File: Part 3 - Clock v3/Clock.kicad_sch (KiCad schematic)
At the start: 77 parts, among them SW2 MODE, SW3 SPEED, SW4 STEP, SW5 BOOT SPEED, SW6 BOOT MODE, SW7 SW_DIP_x08, SW8 RESET FAST LSB, SW9 RESET FAST MSB, U1 74AHC14, U10 74HC112, U11 74AHC74, U12 LMC555, U13 74HC251, U14 74HC40103, U15 74AHC138, U16 74HC251, U17 74HC251, U3 74AHC08, U4 74AHC14, U5 74AHC74, U6 74AHC74, U7 74AHC74, U8 74AHC74, U9 74HC112, X1 14.7456MHz

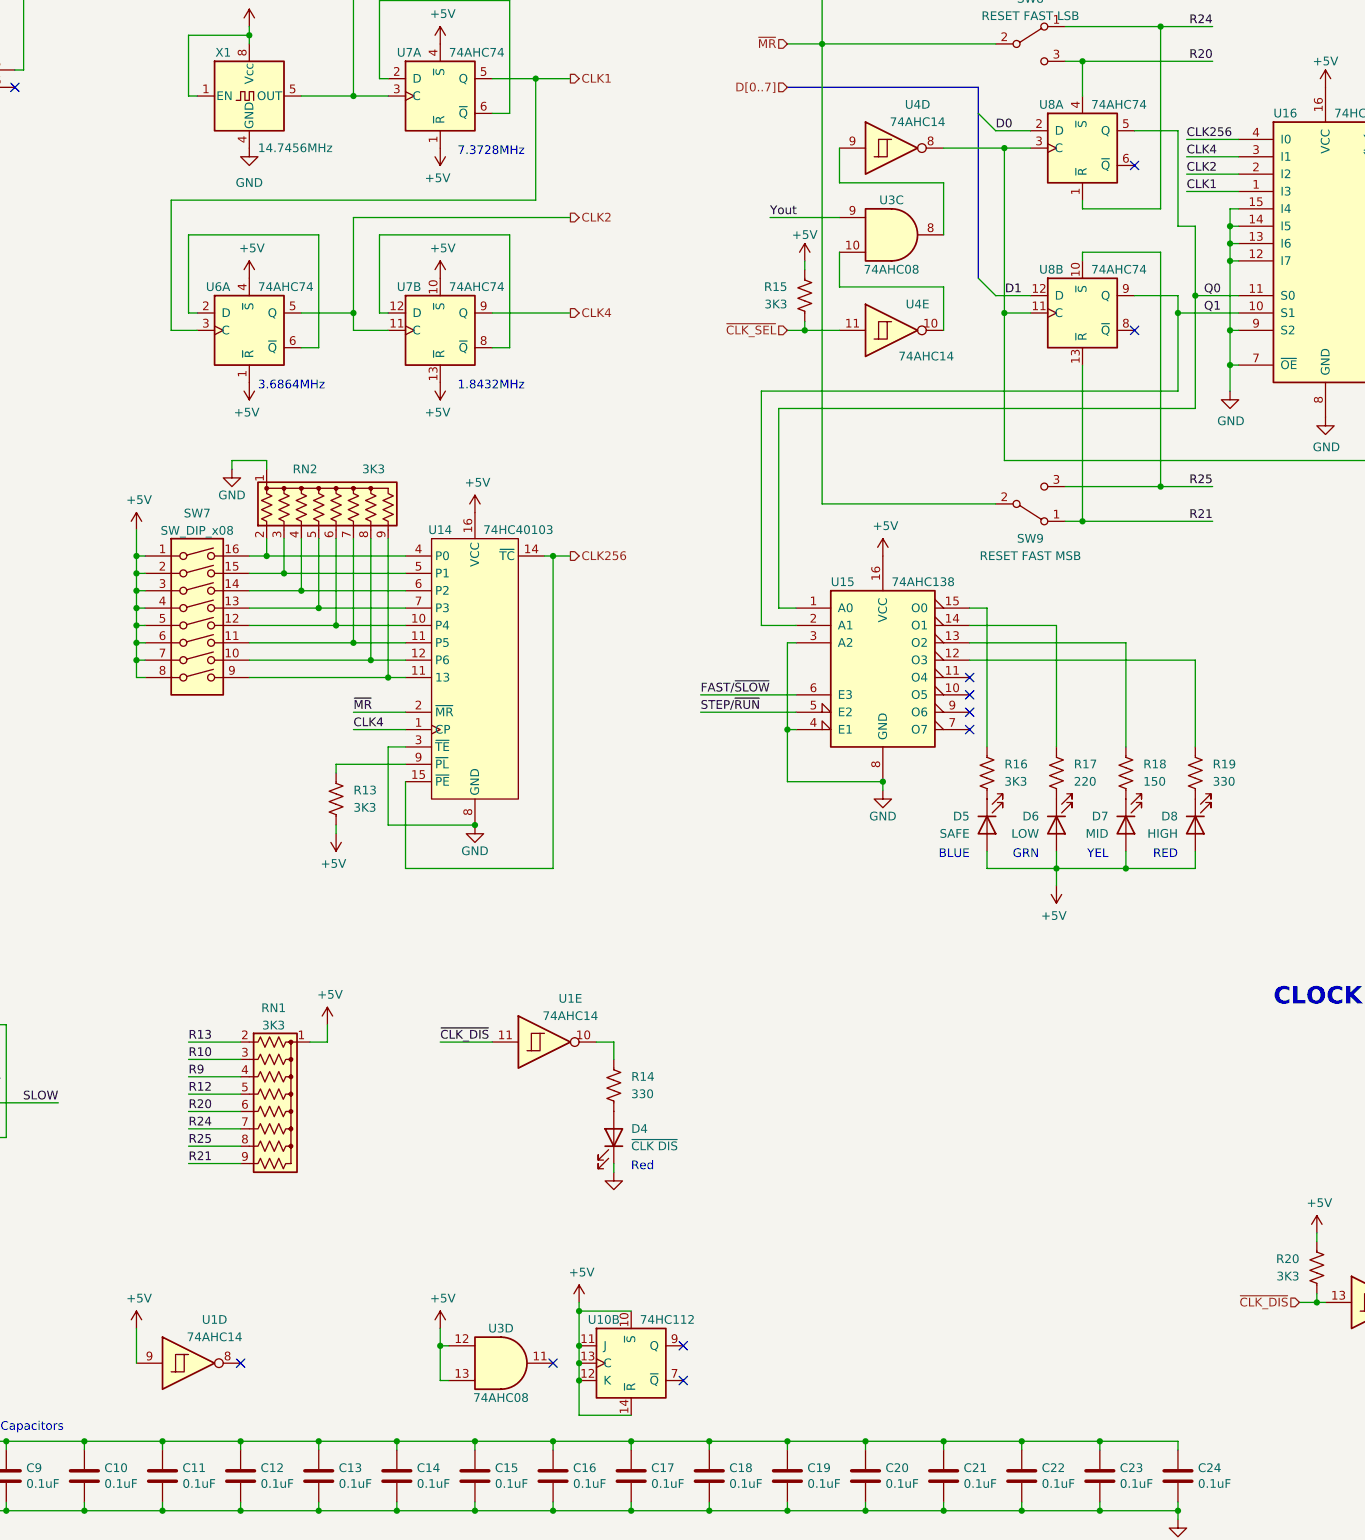
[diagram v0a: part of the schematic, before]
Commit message: Attempted to reduce chip count
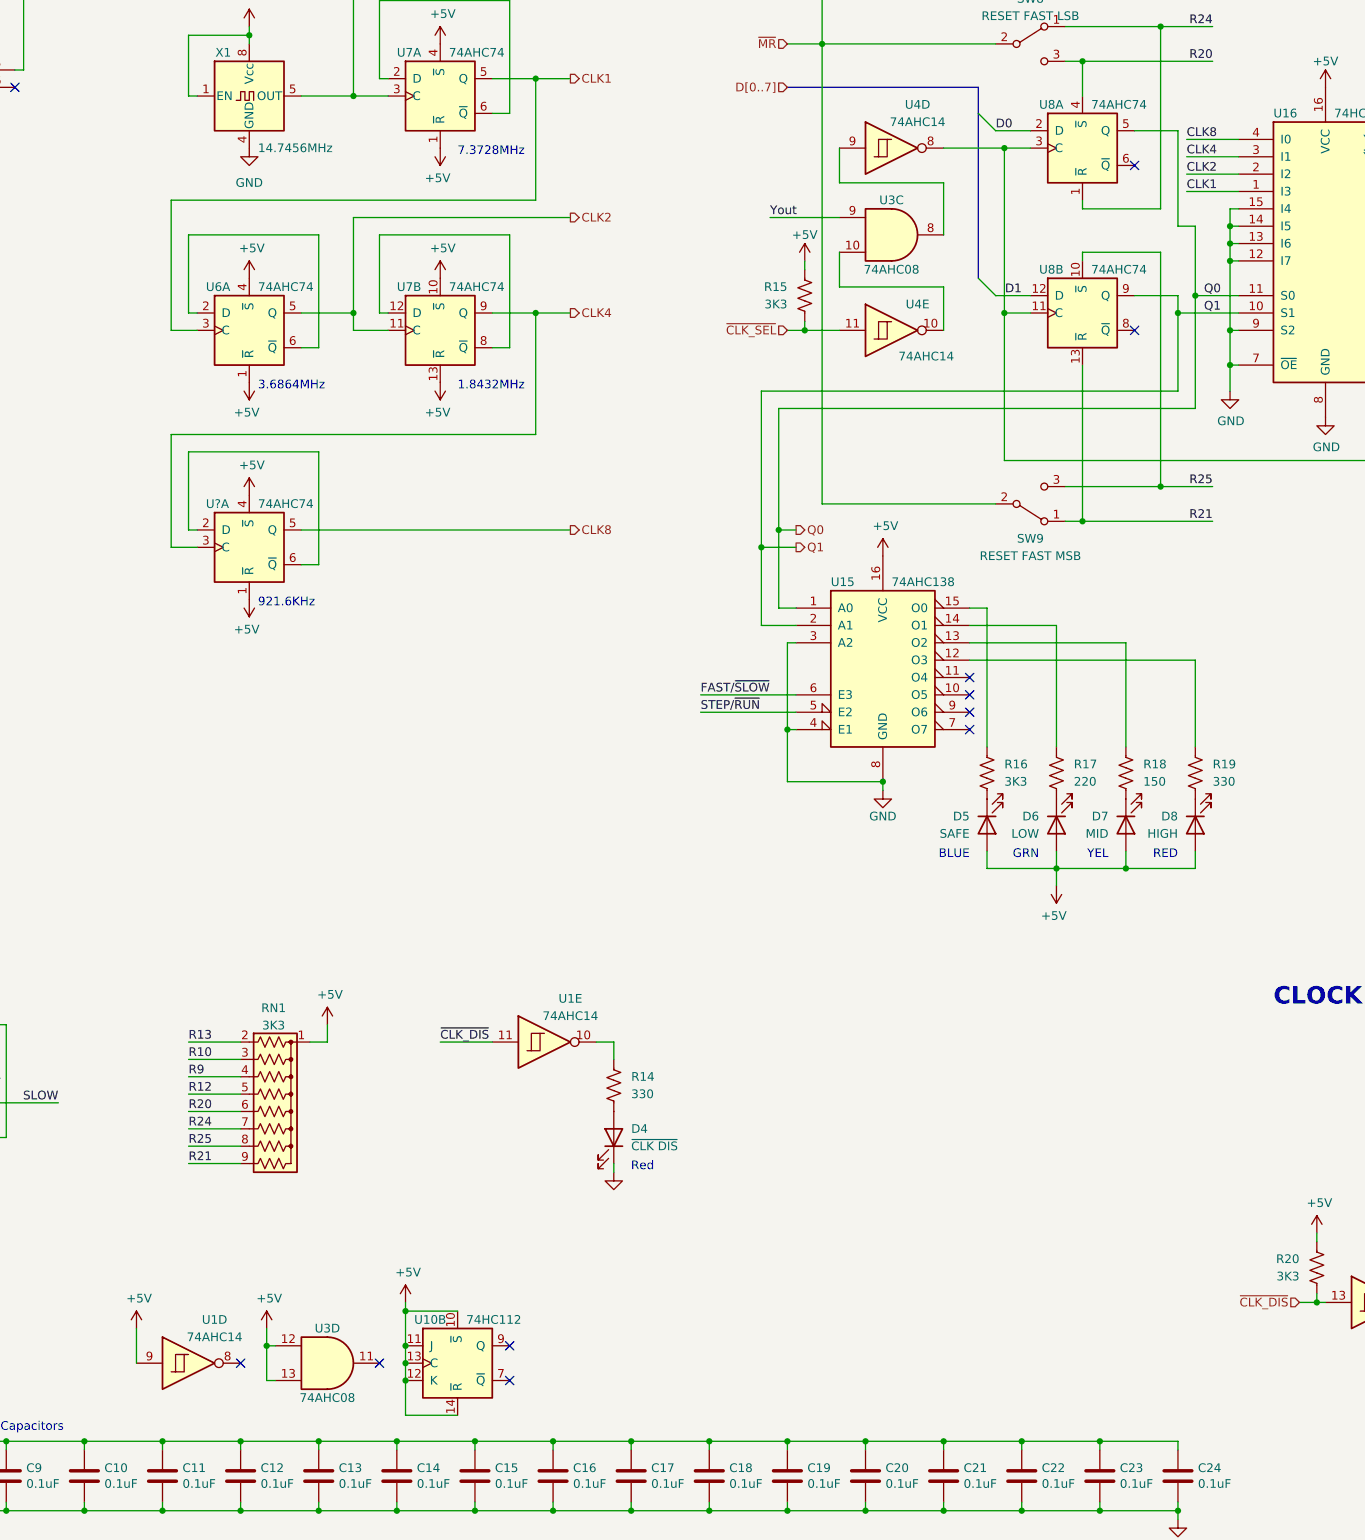
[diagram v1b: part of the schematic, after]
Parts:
- removed R13: 3K3, Resistor_THT:R_Axial_DIN0207_L6.3mm_D2.5mm_P10.16mm_Horizontal, symbol Device:R_US
- removed RN2: 3K3, Resistor_THT:R_Array_SIP9, symbol Device:R_Network08_US
- removed SW7: SW_DIP_x08, Button_Switch_THT:SW_DIP_SPSTx08_Slide_6.7x21.88mm_W7.62mm_P2.54mm_LowProfile, symbol Switch:SW_DIP_x08
- removed U14: 74HC40103, Package_DIP:DIP-16_W7.62mm_Socket, symbol 0_Z80_Library:74HC40103
- added U?: 74AHC74, Package_DIP:DIP-14_W7.62mm_Socket, symbol 74xx:74HC74
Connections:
- net +5V: now also U?.1 (~{R}), U?.4 (~{S})
- net CLK4: now also U?.3 (C)
- net CLK256 renamed CLK8
- net CLK8: now also U?.5 (Q)
- new net: U?.2 (D), U?.6 (~{Q})
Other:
- note added: "921.6KHz"
- moved on the sheet: U10B, U3D

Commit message: Clock 3 and Keyboard
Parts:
- removed R11, R3, R5, R7: 1K, Resistor_THT:R_Axial_DIN0207_L6.3mm_D2.5mm_P10.16mm_Horizontal, symbol Device:R_US
- removed R15, R20: 3K3, Resistor_THT:R_Axial_DIN0207_L6.3mm_D2.5mm_P10.16mm_Horizontal, symbol Device:R_US
- removed RN1: 3K3, Resistor_THT:R_Array_SIP9, symbol Device:R_Network08_US
- added RN1: 1K, Resistor_THT:R_Array_SIP5, symbol Device:R_Network04_US
- added RN2: 3K3, Resistor_THT:R_Array_SIP11, symbol Device:R_Network10_US
- added unit 3 of U13
- added unit 2 of U13
- RV1: footprint Potentiometer_THT:Potentiometer_Bourns_3006P_Horizontal -> Potentiometer_THT:Potentiometer_Bourns_3296Z_Horizontal
- gave numbers to parts that had none: 1
- renumbered C17 to C10, C10 to C11, C18 to C12, C11 to C13, C19 to C14, C12 to C15, C20 to C16, C13 to C17, C21 to C18, C14 to C19, C22 to C20, C15 to C21, C23 to C22, C16 to C23, D5 to D4, D6 to D5, D7 to D6, D8 to D7, D4 to D8, R17 to R10, R18 to R11, R19 to R12, R14 to R13, R21 to R14, R4 to R3, R6 to R4, R8 to R5, R9 to R6, R10 to R7, R12 to R8, R16 to R9, SW8 to SW7, SW9 to SW8, U13 to U14, U7 to U6, U6 to U7
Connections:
- net +5V: now also U1.11, U6.1 (~{R}), U6.10 (~{S}), U6.13 (~{R}), U6.4 (~{S}), RN1.1 (common), RN2.1 (common), U13.10 (~{S}), U13.11 (C), U13.12 (D), U13.13 (~{R}), U13.14 (VCC); no longer U1.9, U6.1 (~{R}), U6.10 (~{S}), U6.4 (~{S})
- net CLK1: now also U6.9 (Q); no longer U6.5 (Q)
- net GND: now also R14.2, R6.2, R7.2, U13.7 (GND); no longer D2.1 (K), D3.1 (K), D9.1 (K)
- net R10: now also RN2.3 (R2)
- net R12: now also RN2.5 (R4)
- net R13: now also RN2.2 (R1)
- net R20: now also RN2.6 (R5)
- net R21: now also RN2.9 (R8)
- net R24: now also RN2.7 (R6)
- net R25: now also RN2.8 (R7)
- net R9: now also RN2.4 (R3)
- net SLOW: now also U6.5 (Q); no longer U6.9 (Q)
- net ~{CLK_DIS}: now also RN2.10 (R9); no longer U1.11
- net ~{CLK_SEL}: now also RN2.11 (R10)
- net ~{PWR_UP}: no longer U6.13 (~{R})
- net R11: now reaches RV1.3, U12.7 (DIS)
- net R11: now also RN1.5 (R4)
- net at U12.3 (Q): now also U6.3 (C); no longer U6.11 (C)
- net R5: now reaches R4.2, SW3.1
- net R5: now also RN1.3 (R2)
- net at U10.3 (J), U5.5 (Q): now also D3.2 (A); no longer R7.1
- net at U1.10: now also U1.9; no longer R13.1
- net R3: now reaches R3.2, SW2.1
- net R3: now also RN1.2 (R1)
- net at D9.2 (A): now also U4.12; no longer R14.2
- net R7: now reaches R5.2, SW4.1
- net R7: now also RN1.4 (R3)
- net at U1.12, U17.7 (~{OE}): now also R13.1
- net at R14.1: now also D9.1 (K); no longer U4.12
- net at D2.2 (A): now also U5.12 (D), U5.8 (~{Q}), U9.2 (K); no longer R6.2
- net OSC: no longer names the net of X1.5 (OUT)
- net OSC: now also U6.11 (C); no longer U6.3 (C)
- new net: U6.2 (D), U6.6 (~{Q})
- new net: D3.1 (K), R7.1
- new net: D2.1 (K), R6.1
- new net: U6.12 (D), U6.8 (~{Q})
- no-connect marks 16 -> 18
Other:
- moved on the sheet: C10, C11, C12, C13, C14, C15, C16, C17, C18, C19, C20, C21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

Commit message: Added Keyboard, and minor fixes
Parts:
- U1, U4: value 74AHC14 -> 74AC14
- U10, U9: value 74HC112 -> 74AC112
- U11, U13, U5, U6, U7, U8: value 74AHC74 -> 74AC74
- U15: value 74AHC138 -> 74HC138
- U3: value 74AHC08 -> 74AC08
